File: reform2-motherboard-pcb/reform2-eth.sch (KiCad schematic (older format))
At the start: 9 parts, among them P1 J0G-0003NL

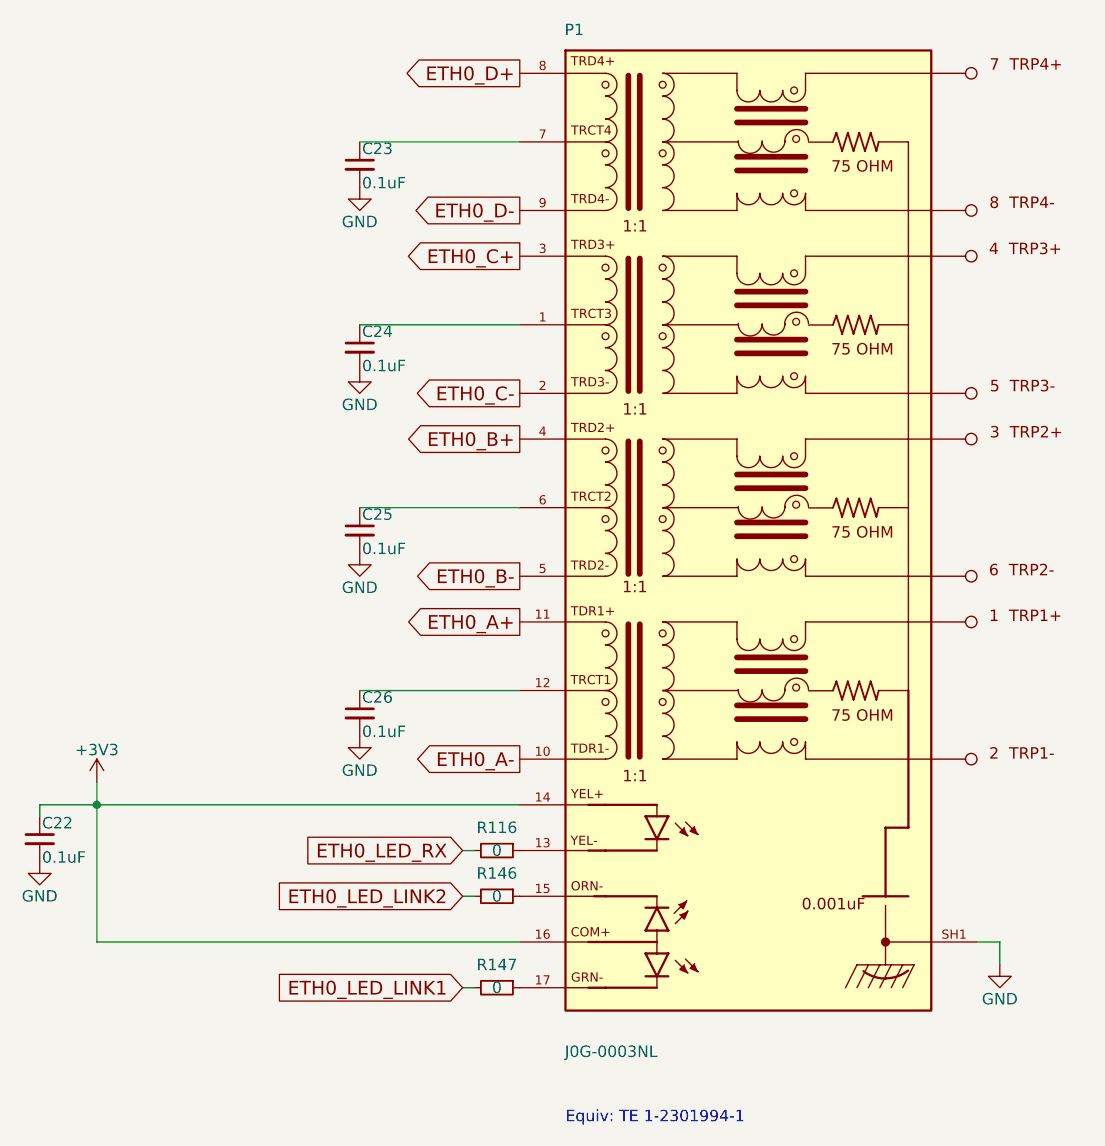
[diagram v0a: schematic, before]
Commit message: motherboard: add the split-up and cleaned up schematics that were made for the book
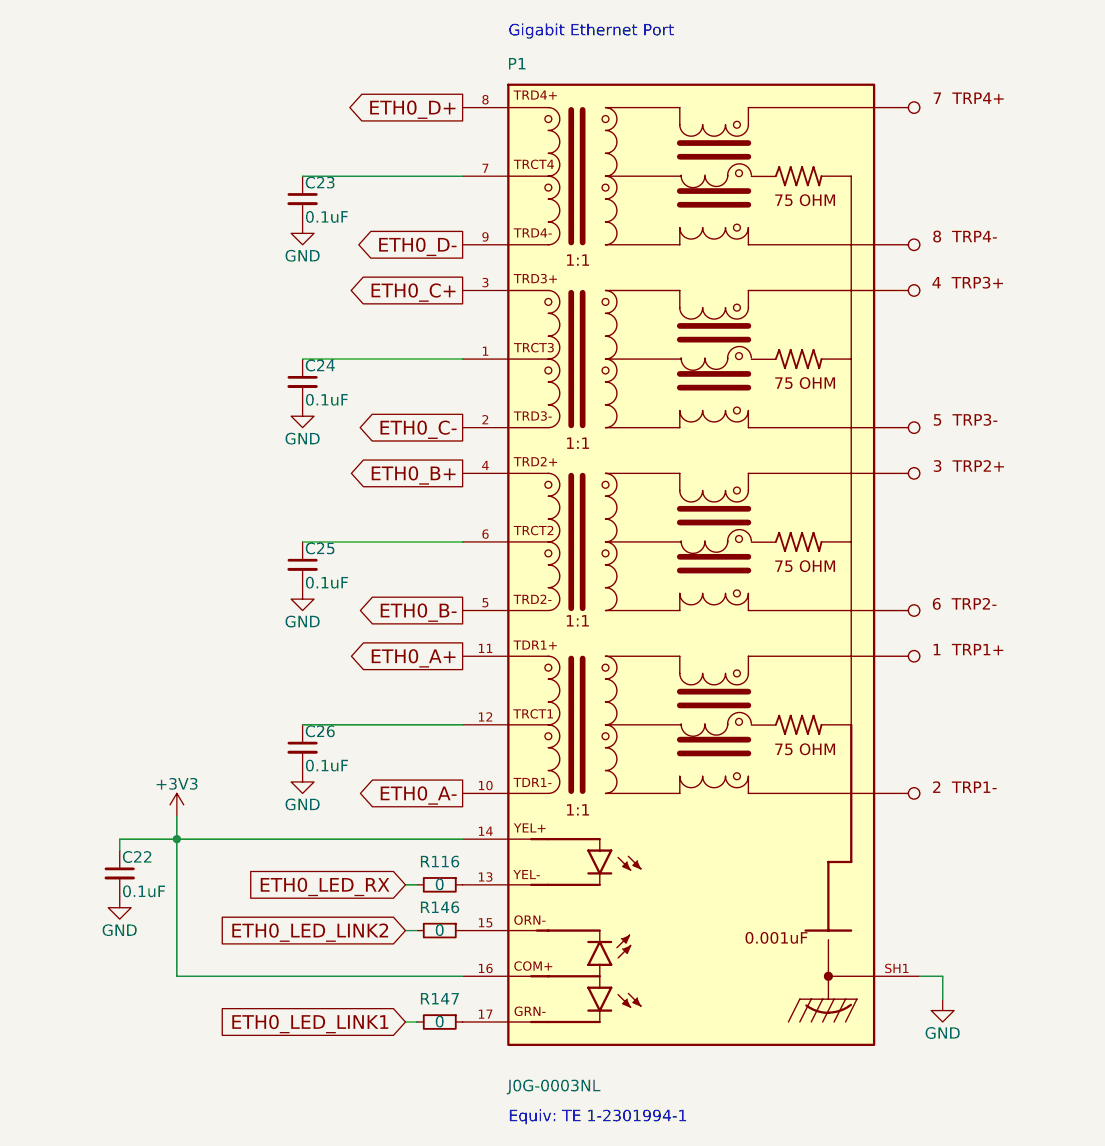
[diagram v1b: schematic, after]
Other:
- note added: "Gigabit Ethernet Port"
- moved on the sheet: C22, C23, C24, C25, C26, P1, R116, R146, R147
